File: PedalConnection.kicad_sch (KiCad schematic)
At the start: 20 parts, among them U10 OPA325IDBVR, U11 OPA325IDBVR, U13 VOM618A-3T, U9 VOM618A-3T

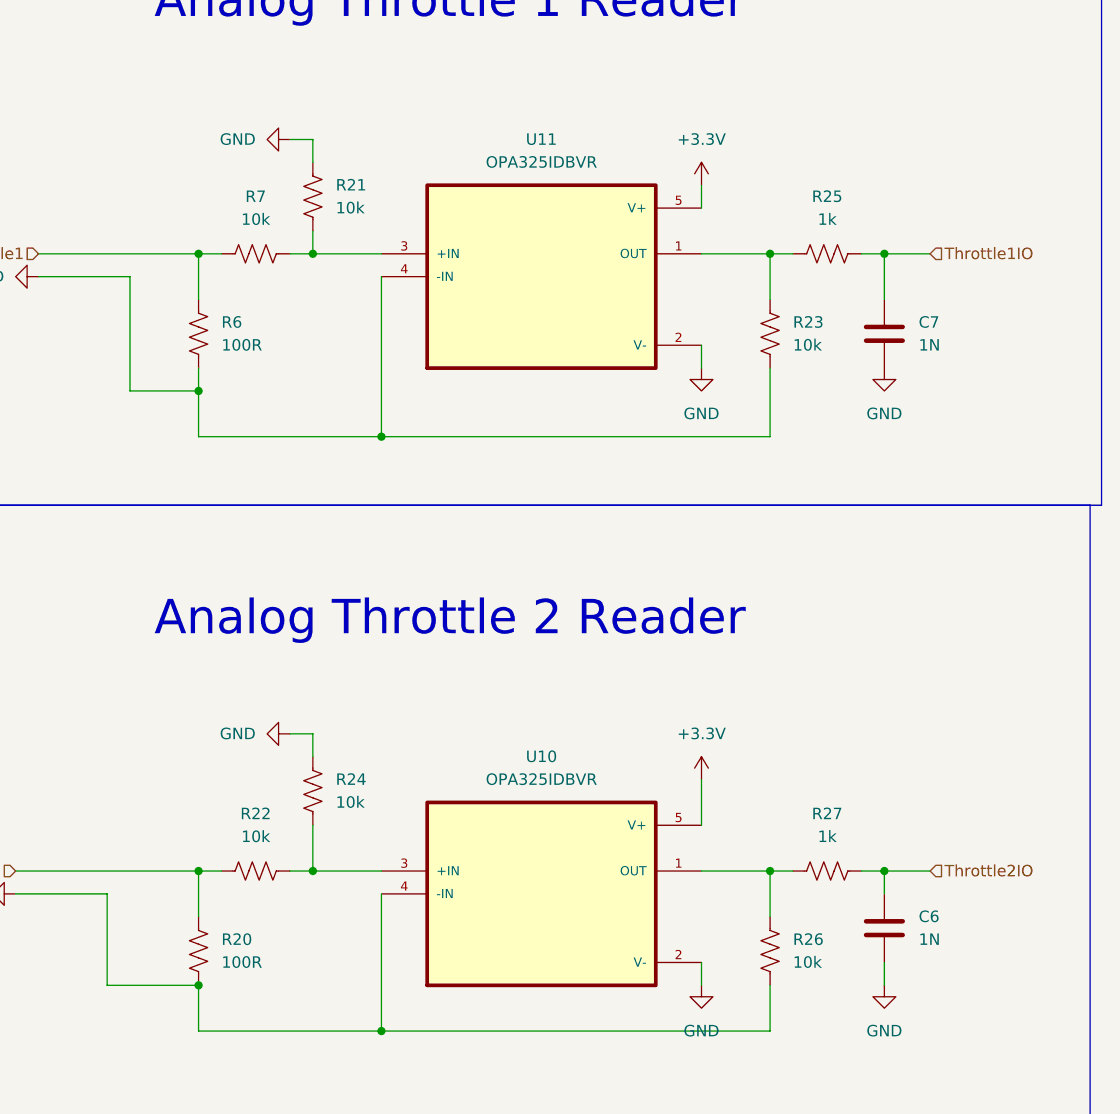
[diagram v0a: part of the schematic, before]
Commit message: front silkscreen
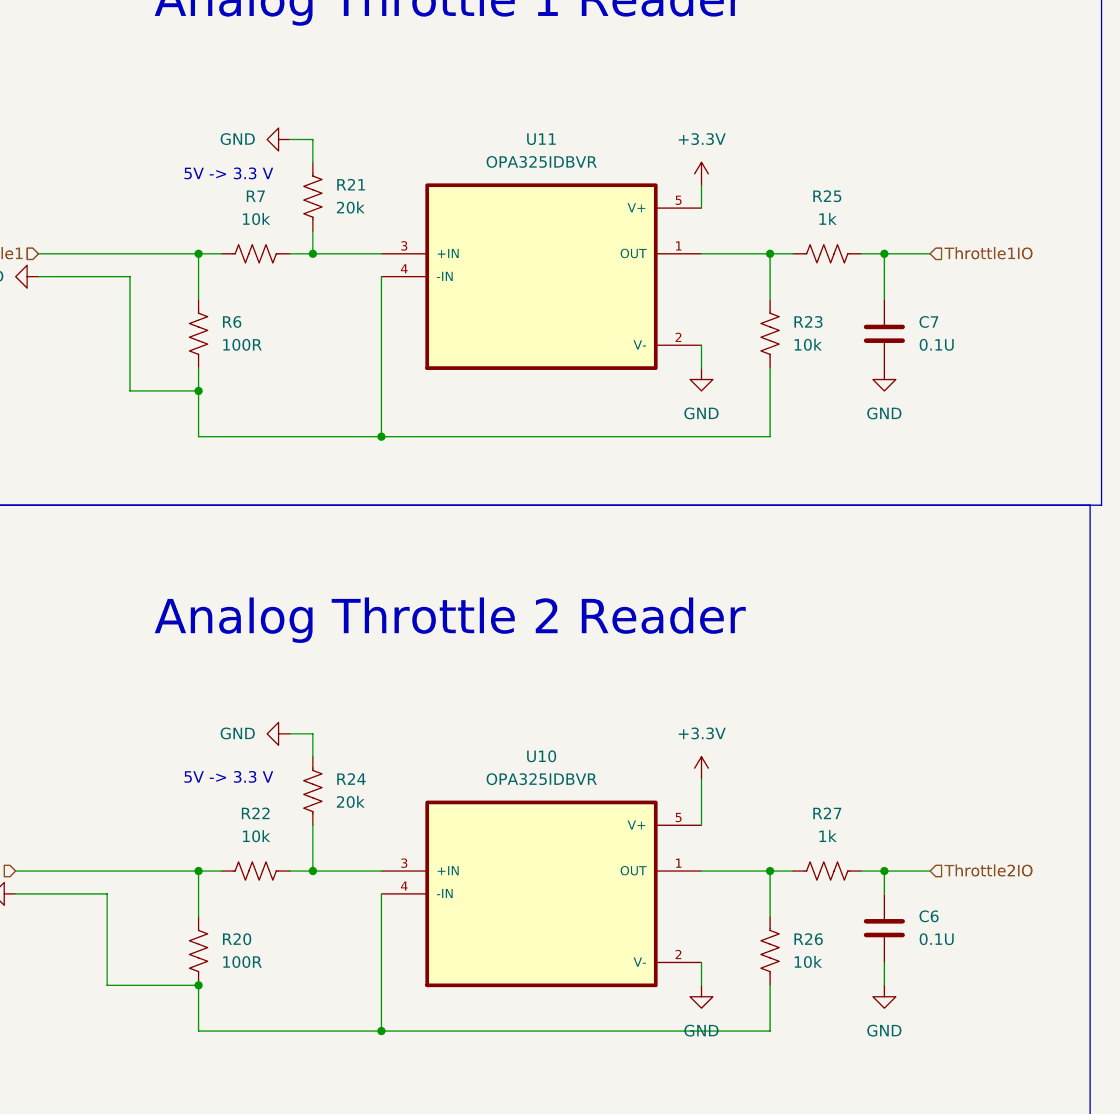
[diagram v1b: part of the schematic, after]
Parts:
- C6, C7: value 1N -> 0.1U
- R21, R24: value 10k -> 20k
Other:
- note added: "5V -> 3.3 V"
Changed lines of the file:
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@@
 		)
 	)
+	(text "5V -> 3.3 V"
+		(exclude_from_sim no)
+		(at 183.642 47.244 0)
+		(effects
+			(font
+				(size 1.27 1.27)
+			)
+		)
+	)
+	(text "5V -> 3.3 V"
+		(exclude_from_sim no)
+		(at 183.642 114.3 0)
+		(effects
+			(font
+				(size 1.27 1.27)
+			)
+		)
+	)
 	(text "Analog Throttle 2 Reader"
 		(exclude_from_sim no)
@@
 			)
 		)
-		(property "Value" "1N"
+		(property "Value" "0.1U"
 			(at 260.35 132.0799 0)
 			(show_name no)
@@
 			)
 		)
-		(property "Value" "1N"
+		(property "Value" "0.1U"
 			(at 260.35 66.0399 0)
 			(show_name no)
@@
 			)
 		)
-		(property "Value" "10k"
+		(property "Value" "20k"
 			(at 195.58 116.8399 0)
 			(show_name no)
@@
 			)
 		)
-		(property "Value" "10k"
+		(property "Value" "20k"
 			(at 195.58 50.7999 0)
 			(show_name no)
